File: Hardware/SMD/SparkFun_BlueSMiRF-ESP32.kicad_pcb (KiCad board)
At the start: 2 copper layers, 38.1 x 15.2 mm, 45 parts, among them J1 Conn_01x06, Q1 Q_NMOS_DGS, Q2 Q_NMOS_DGS, SW1 Switch, U1 ESP32_Pico_Mini, U2 AP2112K-3.3

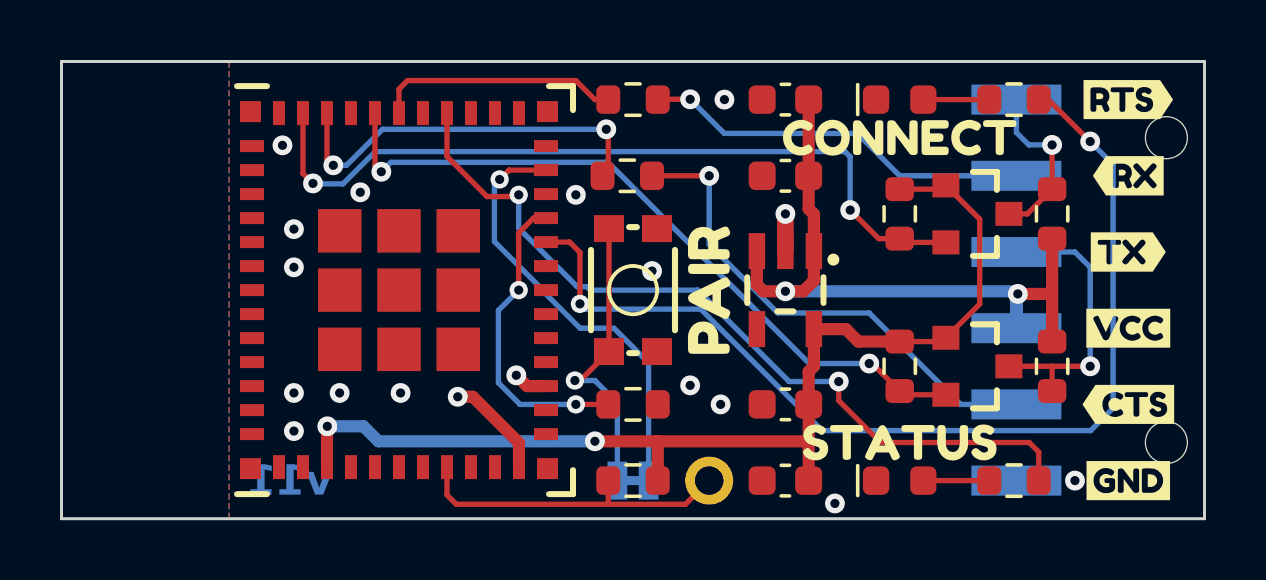
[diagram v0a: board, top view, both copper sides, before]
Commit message: Post design review fixes.
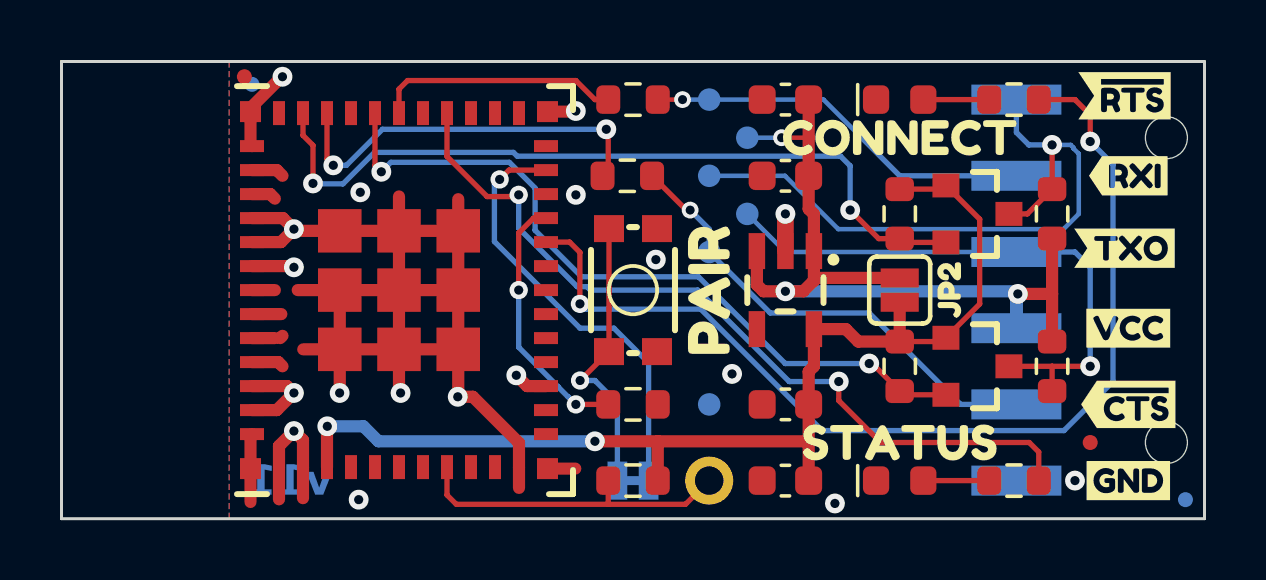
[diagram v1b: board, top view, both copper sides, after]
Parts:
- removed U3: ~, SparkFun-Aesthetic:Ordering_Instructions
- removed kibuzzard-64C48410: G***, kibuzzard-64C48410
- removed kibuzzard-64C4844B: G***, kibuzzard-64C4844B
- removed kibuzzard-64C48496: G***, kibuzzard-64C48496
- removed kibuzzard-64C484A1: G***, kibuzzard-64C484A1
- removed kibuzzard-65022E62: G***, kibuzzard-65022E62
- removed kibuzzard-65022E77: G***, kibuzzard-65022E77
- removed kibuzzard-65022E81: G***, kibuzzard-65022E81
- removed kibuzzard-65022E99: G***, kibuzzard-65022E99
- removed kibuzzard-65022EA5: G***, kibuzzard-65022EA5
- removed kibuzzard-65022EE4: G***, kibuzzard-65022EE4
- added FID1: Fiducial_0.5, SparkFun-Aesthetic:Fiducial_0.5mm_Mask1mm, F.Cu at (163.8, 129.5)
- added FID2: Fiducial_0.5, SparkFun-Aesthetic:Fiducial_0.5mm_Mask1mm, F.Cu at (135.6, 117.3)
- added FID3: Fiducial_0.5, SparkFun-Aesthetic:Fiducial_0.5mm_Mask1mm, B.Cu at (167.0, 131.4)
- added FID4: Fiducial_0.5, SparkFun-Aesthetic:Fiducial_0.5mm_Mask1mm, B.Cu at (135.9, 117.6)
- added JP2: ~, SparkFun-Jumper:SMT-JUMPER_2_NO_SILK, F.Cu at (157.5, 124.5)
- added TP2: TestPoint_0.75mm, SparkFun-Connector:TestPoint-0.75mm, B.Cu at (151.1, 118.1)
- added TP3: TestPoint_0.75mm, SparkFun-Connector:TestPoint-0.75mm, B.Cu at (151.1, 123.2)
- added TP4: TestPoint_0.75mm, SparkFun-Connector:TestPoint-0.75mm, B.Cu at (152.4, 121.9)
- added TP5: TestPoint_0.75mm, SparkFun-Connector:TestPoint-0.75mm, B.Cu at (151.1, 120.7)
- added TP6: TestPoint_0.75mm, SparkFun-Connector:TestPoint-0.75mm, B.Cu at (151.1, 128.3)
- added TP7: TestPoint_0.75mm, SparkFun-Connector:TestPoint-0.75mm, B.Cu at (152.4, 119.4)
- added U7: ~, SparkFun-Aesthetic:Ordering_Instructions, F.Cu at (180.3, 81.3)
- added kibuzzard-65597E65: G***, kibuzzard-65597E65, F.Cu at (165.1, 128.3)
- added kibuzzard-65597EC2: G***, kibuzzard-65597EC2, B.Cu at (157.4, 128.3)
- added kibuzzard-65597EE2: G***, kibuzzard-65597EE2, B.Cu at (157.5, 118.1)
- added kibuzzard-655A4531: G***, kibuzzard-655A4531, F.Cu at (165.1, 120.7)
- added kibuzzard-655A454B: G***, kibuzzard-655A454B, B.Cu at (157.7, 120.7)
- added kibuzzard-655A4561: G***, kibuzzard-655A4561, B.Cu at (157.2, 123.2)
- added kibuzzard-655A45DC: G***, kibuzzard-655A45DC, B.Cu at (153.3, 130.8)
- added kibuzzard-655A5305: G***, kibuzzard-655A5305, B.Cu at (156.6, 125.7)
- added kibuzzard-655A5381: G***, kibuzzard-655A5381, F.Cu at (165.0, 123.1)
- added kibuzzard-655A539C: G***, kibuzzard-655A539C, F.Cu at (165.0, 118.0)
- added kibuzzard-655A5C31: G***, kibuzzard-655A5C31, F.Cu at (159.1, 124.5)
- Q1, Q2: value Q_NMOS_DGS -> NMOS_0.2A_50V
- R10, R3, R4, R7, R8, R9: value 10k -> 1k
- SW1: value Switch -> SPST_Momentary_4.6x2.8mm
- U1: value ESP32_Pico_Mini -> ESP32-PICO-V3-02
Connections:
- net CTS_HV renamed ~{CTS_HV}
- net CTS_LV renamed ~{CTS_LV}
- net RTS_HV renamed ~{RTS_HV}
- net RTS_LV renamed ~{RTS_LV}
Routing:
- net GND: track 6.08 -> 64.5 mm
- net ~{RTS_HV}: track 5.71 -> 22.0 mm
- net TX_HV: track 9.51 -> 19.0 mm
- net VCC: track 24.0 -> 29.0 mm, vias 2 -> 3
- net Net-(U1-IOA15): track 10.3 -> 8.70 mm
- net +3.3V: track 36.3 -> 37.6 mm
- net ~{CTS_HV}: track 16.8 -> 15.7 mm
- net TX_LV: track 24.2 -> 25.0 mm
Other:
- board text added: "Copper Weight: 1oz"
- board text added: "Finish: Lead Free HASL"
- board text added: "Material: TG155"
- board text removed: "Finish: HASL Lead Free"

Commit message: Change BSS138 resistors to 10k
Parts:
- removed U7: ~, SparkFun-Aesthetic:Ordering_Instructions
- added U3: ~, SparkFun-Aesthetic:ORDERING_INSTRUCTIONS, F.Cu at (1.52, 4.06)
- R1: value 4.7k -> 10k
- R10, R7, R8, R9: value 1k -> 10k
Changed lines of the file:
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@@
       (stroke (width 0) (type solid)) (fill solid) (layer "F.SilkS"))
   )
-  (footprint "SparkFun-Aesthetic:Ordering_Instructions" (layer "F.Cu")
-    (at 180.34 81.28)
-    (property "Sheetfile" "SparkFun_Default_KiCad_Setup.kicad_sch")
+  (footprint "SparkFun-Aesthetic:ORDERING_INSTRUCTIONS" (layer "F.Cu")
+    (at 1.52 4.06)
+    (property "Sheetfile" "SparkFun_BlueSMiRF-ESP32.kicad_sch")
     (property "Sheetname" "")
-    (fp_text reference "U7" (at 2.54 -1.27) (layer "F.Fab") hide
+    (fp_text reference "U3" (at 2.54 -1.27) (layer "F.Fab") hide
         (effects (font (size 1.27 1.27) (thickness 0.15)))
     )
@@
         (effects (font (size 1.27 1.27) (thickness 0.15)))
     )
-    (fp_text user "Ordering Instructions:" (at 1.27 1.27) (layer "Cmts.User")
+    (fp_text user "Ordering Instructions:" (at 1.27 1.27) (layer "User.1")
         (effects (font (size 2.5908 2.5908) (thickness 0.4572)) (justify left top))
     )
     (fp_line (start 0 4.445) (end 63.5 4.445)
-      (stroke (width 0.2032) (type solid)) (layer "Cmts.User"))
+      (stroke (width 0.2032) (type solid)) (layer "User.1"))
     (fp_rect (start 0 0) (end 63.5 50.8)
-      (stroke (width 0.2) (type default)) (fill none) (layer "Cmts.User"))
+      (stroke (width 0.2) (type default)) (fill none) (layer "User.1"))
   )
   (footprint "kibuzzard-655A5381" (layer "F.Cu")
@@
     (descr "Resistor SMD 0603 (1608 Metric), square (rectangular) end terminal, IPC_7351 nominal, (Body size source: IPC-SM-782 page 72, https://www.pcb-3d.com/wordpress/wp-content/uploads/ipc-sm-782a_amendment_1_and_2.pdf), generated with kicad-footprint-generator")
     (tags "resistor")
-    (property "PROD_ID" "RES-07856")
+    (property "PROD_ID" "RES-00824")
     (property "Sheetfile" "SparkFun_BlueSMiRF-ESP32.kicad_sch")
     (property "Sheetname" "")
@@
         (effects (font (size 0.5 0.5) (thickness 0.1) bold))
     )
-    (fp_text value "1k" (at 0 1.43 90) (layer "F.Fab")
+    (fp_text value "10k" (at 0 1.43 90) (layer "F.Fab")
         (effects (font (size 0.5 0.5) (thickness 0.1) bold))
     )
@@
     (descr "Resistor SMD 0603 (1608 Metric), square (rectangular) end terminal, IPC_7351 nominal, (Body size source: IPC-SM-782 page 72, https://www.pcb-3d.com/wordpress/wp-content/uploads/ipc-sm-782a_amendment_1_and_2.pdf), generated with kicad-footprint-generator")
     (tags "resistor")
-    (property "PROD_ID" "RES-07857")
+    (property "PROD_ID" "RES-00824")
     (property "Sheetfile" "SparkFun_BlueSMiRF-ESP32.kicad_sch")
     (property "Sheetname" "")
@@
         (effects (font (size 0.5 0.5) (thickness 0.1) bold))
     )
-    (fp_text value "4.7k" (at 0 1.43) (layer "F.Fab")
+    (fp_text value "10k" (at 0 1.43) (layer "F.Fab")
         (effects (font (size 0.5 0.5) (thickness 0.1) bold))
     )
@@
     (descr "Resistor SMD 0603 (1608 Metric), square (rectangular) end terminal, IPC_7351 nominal, (Body size source: IPC-SM-782 page 72, https://www.pcb-3d.com/wordpress/wp-content/uploads/ipc-sm-782a_amendment_1_and_2.pdf), generated with kicad-footprint-generator")
     (tags "resistor")
-    (property "PROD_ID" "RES-07856")
+    (property "PROD_ID" "RES-00824")
     (property "Sheetfile" "SparkFun_BlueSMiRF-ESP32.kicad_sch")
     (property "Sheetname" "")
@@
         (effects (font (size 0.5 0.5) (thickness 0.1) bold))
     )
-    (fp_text value "1k" (at 0 1.43 90) (layer "F.Fab")
+    (fp_text value "10k" (at 0 1.43 90) (layer "F.Fab")
         (effects (font (size 0.5 0.5) (thickness 0.1) bold))
     )
@@
     (descr "Resistor SMD 0603 (1608 Metric), square (rectangular) end terminal, IPC_7351 nominal, (Body size source: IPC-SM-782 page 72, https://www.pcb-3d.com/wordpress/wp-content/uploads/ipc-sm-782a_amendment_1_and_2.pdf), generated with kicad-footprint-generator")
     (tags "resistor")
-    (property "PROD_ID" "RES-07856")
+    (property "PROD_ID" "RES-00824")
     (property "Sheetfile" "SparkFun_BlueSMiRF-ESP32.kicad_sch")
     (property "Sheetname" "")
@@
         (effects (font (size 0.5 0.5) (thickness 0.1) bold))
     )
-    (fp_text value "1k" (at 0 1.43 90) (layer "F.Fab")
+    (fp_text value "10k" (at 0 1.43 90) (layer "F.Fab")
         (effects (font (size 0.5 0.5) (thickness 0.1) bold))
     )
@@
     (descr "Resistor SMD 0603 (1608 Metric), square (rectangular) end terminal, IPC_7351 nominal, (Body size source: IPC-SM-782 page 72, https://www.pcb-3d.com/wordpress/wp-content/uploads/ipc-sm-782a_amendment_1_and_2.pdf), generated with kicad-footprint-generator")
     (tags "resistor")
-    (property "PROD_ID" "RES-07856")
+    (property "PROD_ID" "RES-00824")
     (property "Sheetfile" "SparkFun_BlueSMiRF-ESP32.kicad_sch")
     (property "Sheetname" "")
@@
         (effects (font (size 0.5 0.5) (thickness 0.1) bold))
     )
-    (fp_text value "1k" (at 0 1.43 90) (layer "F.Fab")
+    (fp_text value "10k" (at 0 1.43 90) (layer "F.Fab")
         (effects (font (size 0.5 0.5) (thickness 0.1) bold))
     )
@@
     (pts (xy 129.54 116.84) (xy 173.736 116.84))
     (height -3.302)
-    (gr_text "1.74 in" (at 151.638 112.388) (layer "User.1")
+    (gr_text "44.2 mm" (at 151.638 112.388) (layer "User.1")
       (effects (font (size 1 1) (thickness 0.15)))
     )
@@
     (pts (xy 173.62 130.81) (xy 173.62 118.11))
     (height 3.672)
-    (gr_text "0.50 in" (at 176.142 124.46 90) (layer "User.1")
+    (gr_text "12.7 mm" (at 176.142 124.46 90) (layer "User.1")
       (effects (font (size 1 1) (thickness 0.15)))
     )
@@
     (pts (xy 129.54 132.08) (xy 129.54 116.84))
     (height -2.54)
-    (gr_text "0.60 in" (at 125.85 124.46 90) (layer "User.1")
+    (gr_text "15.2 mm" (at 125.85 124.46 90) (layer "User.1")
       (effects (font (size 1 1) (thickness 0.15)))
     )
@@
     (pts (xy 167.64 132.08) (xy 129.54 132.08))
     (height -2.54)
-    (gr_text "1.50 in" (at 148.59 133.47) (layer "User.1")
+    (gr_text "38.1 mm" (at 148.59 133.47) (layer "User.1")
       (effects (font (size 1 1) (thickness 0.15)))
     )
